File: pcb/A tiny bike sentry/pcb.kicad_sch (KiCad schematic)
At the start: 9 parts, among them SW1 SW_Push, U1 ATtiny85-20P

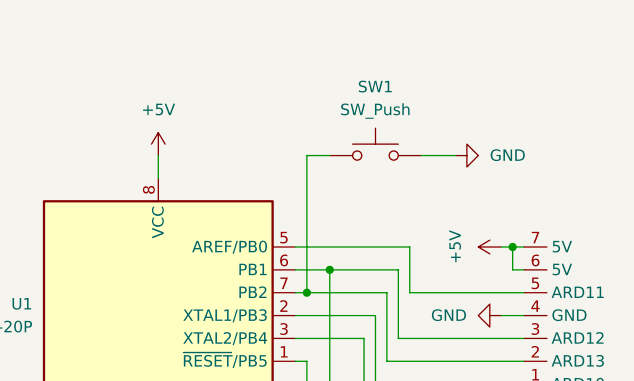
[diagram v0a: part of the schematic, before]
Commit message: Add first draft of Entwicklerdokumentation
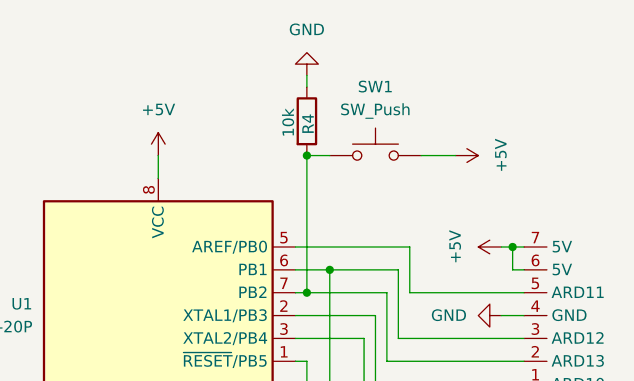
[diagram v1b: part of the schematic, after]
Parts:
- added R4: 10k, Resistor_THT:R_Axial_DIN0207_L6.3mm_D2.5mm_P10.16mm_Horizontal, symbol Device:R
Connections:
- net +5V: now also SW1.2
- net GND: now also R4.1; no longer SW1.2
- net at SW1.1, U1.7 (PB2), U2.2 (ARD13): now also R4.2
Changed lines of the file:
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@@
+	)
+	(junction
+		(at 147.32 66.04)
+		(diameter 0)
+		(color 0 0 0 0)
 	)
 	(junction
@@
 	(wire
 		(pts
+			(xy 147.32 57.15) (xy 147.32 58.42)
+		)
+		(stroke
+			(width 0)
+			(type default)
+		)
+	)
+	(wire
+		(pts
 			(xy 167.64 111.76) (xy 167.64 107.95)
 		)
@@
 	)
 	(symbol
-		(lib_id "power:GND")
-		(at 163.83 66.04 90)
-		(unit 1)
-		(exclude_from_sim no)
-		(in_bom yes)
-		(on_board yes)
-		(dnp no)
-		(fields_autoplaced yes)
-		(property "Reference" "#PWR08"
-			(at 170.18 66.04 0)
-			(effects
-				(font
-					(size 1.27 1.27)
-				)
-				(hide yes)
-			)
-		)
-		(property "Value" "GND"
-			(at 167.64 66.0399 90)
-			(effects
-				(font
-					(size 1.27 1.27)
-				)
-				(justify right)
-			)
-		)
-		(property "Footprint" ""
-			(at 163.83 66.04 0)
-			(effects
-				(font
-					(size 1.27 1.27)
-				)
-				(hide yes)
-			)
-		)
-		(property "Datasheet" ""
-			(at 163.83 66.04 0)
-			(effects
-				(font
-					(size 1.27 1.27)
-				)
-				(hide yes)
-			)
-		)
-		(property "Description" "Power symbol creates a global label with name \"GND\" , ground"
-			(at 163.83 66.04 0)
-			(effects
-				(font
-					(size 1.27 1.27)
-				)
-				(hide yes)
-			)
-		)
-		(pin "1"
-		)
-		(instances
-			(project "pcb"
-				(path "/ac384b63-63a8-4a7a-8e95-96ebce3e1434"
-					(reference "#PWR08")
-					(unit 1)
-				)
-			)
-		)
-	)
-	(symbol
 		(lib_id "MCU_Microchip_ATtiny:ATtiny85-20P")
 		(at 130.81 83.82 0)
@@
 	)
 	(symbol
+		(lib_id "Device:R")
+		(at 147.32 62.23 0)
+		(unit 1)
+		(exclude_from_sim no)
+		(in_bom yes)
+		(on_board yes)
+		(dnp no)
+		(property "Reference" "R4"
+			(at 147.4909 63.6938 90)
+			(effects
+				(font
+					(size 1.27 1.27)
+				)
+				(justify left)
+			)
+		)
+		(property "Value" "10k"
+			(at 145.288 64.008 90)
+			(effects
+				(font
+					(size 1.27 1.27)
+				)
+				(justify left)
+			)
+		)
+		(property "Footprint" "Resistor_THT:R_Axial_DIN0207_L6.3mm_D2.5mm_P10.16mm_Horizontal"
+			(at 145.542 62.23 90)
+			(effects
+				(font
+					(size 1.27 1.27)
+				)
+				(hide yes)
+			)
+		)
+		(property "Datasheet" "~"
+			(at 147.32 62.23 0)
+			(effects
+				(font
+					(size 1.27 1.27)
+				)
+				(hide yes)
+			)
+		)
+		(property "Description" "Resistor"
+			(at 147.32 62.23 0)
+			(effects
+				(font
+					(size 1.27 1.27)
+				)
+				(hide yes)
+			)
+		)
+		(pin "1"
+		)
+		(pin "2"
+		)
+		(instances
+			(project "pcb"
+				(path "/ac384b63-63a8-4a7a-8e95-96ebce3e1434"
+					(reference "R4")
+					(unit 1)
+				)
+			)
+		)
+	)
+	(symbol
 		(lib_id "power:GND")
 		(at 156.21 128.27 0)
@@
 	)
 	(symbol
+		(lib_id "power:GND")
+		(at 147.32 57.15 180)
+		(unit 1)
+		(exclude_from_sim no)
+		(in_bom yes)
+		(on_board yes)
+		(dnp no)
+		(fields_autoplaced yes)
+		(property "Reference" "#PWR08"
+			(at 147.32 50.8 0)
+			(effects
+				(font
+					(size 1.27 1.27)
+				)
+				(hide yes)
+			)
+		)
+		(property "Value" "GND"
+			(at 147.32 52.07 0)
+			(effects
+				(font
+					(size 1.27 1.27)
+				)
+			)
+		)
+		(property "Footprint" ""
+			(at 147.32 57.15 0)
+			(effects
+				(font
+					(size 1.27 1.27)
+				)
+				(hide yes)
+			)
+		)
+		(property "Datasheet" ""
+			(at 147.32 57.15 0)
+			(effects
+				(font
+					(size 1.27 1.27)
+				)
+				(hide yes)
+			)
+		)
+		(property "Description" "Power symbol creates a global label with name \"GND\" , ground"
+			(at 147.32 57.15 0)
+			(effects
+				(font
+					(size 1.27 1.27)
+				)
+				(hide yes)
+			)
+		)
+		(pin "1"
+		)
+		(instances
+			(project "pcb"
+				(path "/ac384b63-63a8-4a7a-8e95-96ebce3e1434"
+					(reference "#PWR08")
+					(unit 1)
+				)
+			)
+		)
+	)
+	(symbol
 		(lib_id "Device:R")
 		(at 162.56 104.14 180)
@@
 					(unit 1)
 				)
+			)
+		)
+	)
+	(symbol
+		(lib_id "power:+5V")
+		(at 163.83 66.04 270)
+		(mirror x)
+		(unit 1)
+		(exclude_from_sim no)
+		(in_bom yes)
+		(on_board yes)
+		(dnp no)
+		(property "Reference" "#PWR09"
+			(at 160.02 66.04 0)
+			(effects
+				(font
+					(size 1.27 1.27)
+				)
+				(hide yes)
+			)
+		)
+		(property "Value" "+5V"
+			(at 168.91 66.04 0)
+			(effects
+				(font
+					(size 1.27 1.27)
+				)
+			)
+		)
+		(property "Footprint" ""
+			(at 163.83 66.04 0)
+			(effects
+				(font
+					(size 1.27 1.27)
+				)
+				(hide yes)
+			)
+		)
+		(property "Datasheet" ""
+			(at 163.83 66.04 0)
+			(effects
+				(font
+					(size 1.27 1.27)
+				)
+				(hide yes)
+			)
+		)
+		(property "Description" "Power symbol creates a global label with name \"+5V\""
+			(at 163.83 66.04 0)
+			(effects
+				(font
+					(size 1.27 1.27)
+				)
+				(hide yes)
+			)
+		)
+		(pin "1"
+		)
+		(instances
+			(project "pcb"
+				(path "/ac384b63-63a8-4a7a-8e95-96ebce3e1434"
+					(reference "#PWR09")
+					(unit 1)
+				)
